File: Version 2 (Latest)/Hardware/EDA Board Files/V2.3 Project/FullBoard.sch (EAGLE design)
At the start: 187 parts, among them IC1 LM3914V, IC2 SGTL5000XNAA3, IC4 MCP73113-16SI_MF, IC5 NCP163ASN330T1G, J1 SJ-3524-SMT-TR, J10 SJ-3524-SMT-TR, J2 Teensy2, J3 Teensy1, J4 SJ-3524-SMT-TR, J7 1981584-1, J9 SJ-3524-SMT-TR, Q2 DMG9926USD-13, SW1 GATERON_LOW_PROFILE, SW10 GATERON_LOW_PROFILE, SW11 GATERON_LOW_PROFILE, SW12 GATERON_LOW_PROFILE, SW13 GATERON_LOW_PROFILE, SW14 GATERON_LOW_PROFILE, SW15 GATERON_LOW_PROFILE, SW16 GATERON_LOW_PROFILE, SW17 GATERON_LOW_PROFILE, SW18 GATERON_LOW_PROFILE, SW19 GATERON_LOW_PROFILE, SW2 GATERON_LOW_PROFILE, SW20 GATERON_LOW_PROFILE, SW21 GATERON_LOW_PROFILE, SW22 GATERON_LOW_PROFILE, SW23 GATERON_LOW_PROFILE, SW24 GATERON_LOW_PROFILE, SW25 GATERON_LOW_PROFILE, SW26 GATERON_LOW_PROFILE, SW27 GATERON_LOW_PROFILE, SW28 GATERON_LOW_PROFILE, SW29 GATERON_LOW_PROFILE, SW3 GATERON_LOW_PROFILE, SW30 GATERON_LOW_PROFILE, SW31 GATERON_LOW_PROFILE, SW32 GATERON_LOW_PROFILE, SW33 GATERON_LOW_PROFILE, SW34 GATERON_LOW_PROFILE, SW35 GATERON_LOW_PROFILE, SW36 GATERON_LOW_PROFILE, SW37 GATERON_LOW_PROFILE, SW38 GATERON_LOW_PROFILE, SW39 GATERON_LOW_PROFILE, SW4 GATERON_LOW_PROFILE, SW40 GATERON_LOW_PROFILE, SW41 GATERON_LOW_PROFILE, SW42 GATERON_LOW_PROFILE, SW43 GATERON_LOW_PROFILE, SW44 GATERON_LOW_PROFILE, SW45 GATERON_LOW_PROFILE, SW46 GATERON_LOW_PROFILE, SW47 GATERON_LOW_PROFILE, SW5 GATERON_LOW_PROFILE, SW6 GATERON_LOW_PROFILE, SW7 GATERON_LOW_PROFILE, SW8 GATERON_LOW_PROFILE, SW9 GATERON_LOW_PROFILE, U1 W25Q128FVSIG, U2 ATMEGA4809-AFR, U3 PAM2401, U4 MAX6775XKA+21-0076E_MXM-M, U5 AP7313-15SAG-7SOT-23_DIO-L, U6 S25FL512SAGMFIR13SO3016_SPA-M

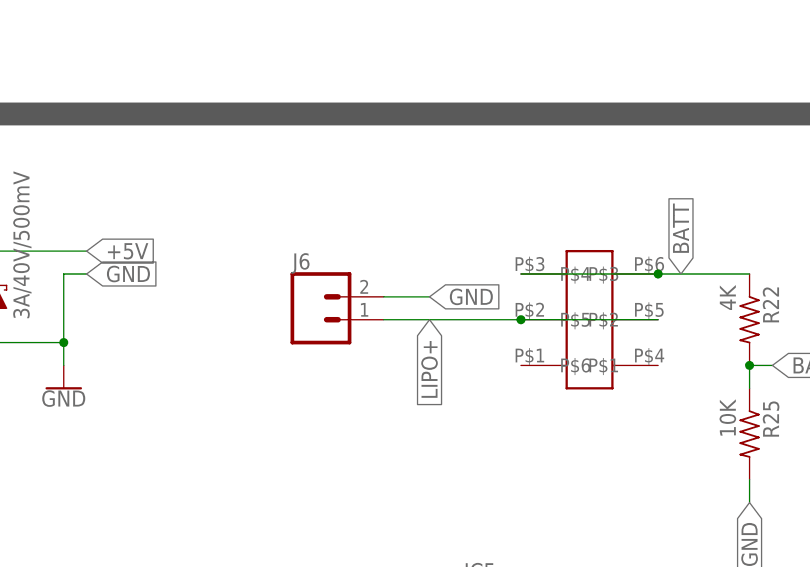
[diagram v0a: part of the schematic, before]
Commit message: Updated battery connector on PCB
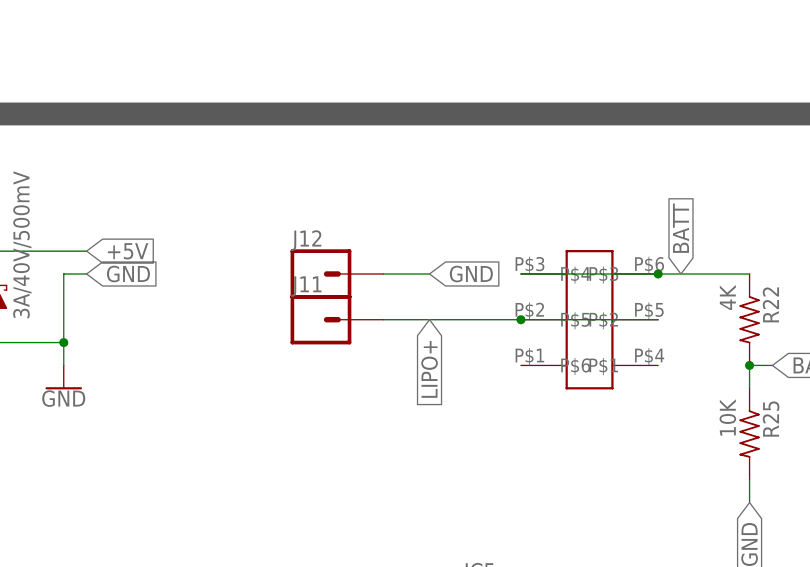
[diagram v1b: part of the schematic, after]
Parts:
- removed J6: (no value), SparkFun-Connectors:CONN_02
- added J11, J12: (no value), SparkFun-Connectors:CONN_01
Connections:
- net GND: now also J12.1; no longer J6.2
- net LIPO+: now also J11.1; no longer J6.1
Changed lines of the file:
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@@
 <part name="C22" library="SparkFun-Capacitors" library_urn="urn:adsk.eagle:library:510" deviceset="22UF" device="-0805-6.3V-20%" package3d_urn="urn:adsk.eagle:package:37429/1" value="22uF"/>
 <part name="CHARGE" library="adafruit" library_urn="urn:adsk.eagle:library:420" deviceset="LED" device="CHIPLED_0805" package3d_urn="urn:adsk.eagle:package:6240559/1"/>
-<part name="J6" library="SparkFun-Connectors" deviceset="CONN_02" device=""/>
 <part name="U4" library="BatteryStuff" deviceset="MAX6775XKA+" device="21-0076E_MXM-M"/>
 <part name="R21" library="adafruit" library_urn="urn:adsk.eagle:library:420" deviceset="R-US_" device="M0805" package3d_urn="urn:adsk.eagle:package:6240587/1" value="3.2M"/>
@@
 <part name="TP3" library="SparkFun-Connectors" library_urn="urn:adsk.eagle:library:513" deviceset="TEST-POINT" device="3X5" package3d_urn="urn:adsk.eagle:package:38285/1"/>
 <part name="TP4" library="SparkFun-Connectors" library_urn="urn:adsk.eagle:library:513" deviceset="TEST-POINT" device="3X5" package3d_urn="urn:adsk.eagle:package:38285/1"/>
+<part name="J11" library="SparkFun-Connectors" library_urn="urn:adsk.eagle:library:513" deviceset="CONN_01" device="" package3d_urn="urn:adsk.eagle:package:38028/1"/>
+<part name="J12" library="SparkFun-Connectors" library_urn="urn:adsk.eagle:library:513" deviceset="CONN_01" device="" package3d_urn="urn:adsk.eagle:package:38028/1"/>
 </parts>
 <sheets>
@@
 <attribute name="VALUE" x="-38.608" y="-235.585" size="1.778" layer="96" rot="R180"/>
 </instance>
-<instance part="J6" gate="G$1" x="-86.36" y="-144.78" smashed="yes">
-<attribute name="VALUE" x="-88.9" y="-149.606" size="1.778" layer="96" font="vector"/>
-<attribute name="NAME" x="-88.9" y="-139.192" size="1.778" layer="95" font="vector"/>
-</instance>
 <instance part="U4" gate="A" x="-241.3" y="-226.06" smashed="yes">
 <attribute name="NAME" x="-215.5444" y="-216.9414" size="2.0828" layer="95" ratio="6" rot="SR0"/>
@@
 <attribute name="NAME" x="-48.26" y="-73.66" size="1.778" layer="95" font="vector"/>
 <attribute name="VALUE" x="-48.26" y="-78.74" size="1.778" layer="96" font="vector"/>
+</instance>
+<instance part="J11" gate="G$1" x="-86.36" y="-144.78" smashed="yes">
+<attribute name="VALUE" x="-88.9" y="-149.606" size="1.778" layer="96" font="vector"/>
+<attribute name="NAME" x="-88.9" y="-141.732" size="1.778" layer="95" font="vector"/>
+</instance>
+<instance part="J12" gate="G$1" x="-86.36" y="-139.7" smashed="yes">
+<attribute name="VALUE" x="-88.9" y="-144.526" size="1.778" layer="96" font="vector"/>
+<attribute name="NAME" x="-88.9" y="-136.652" size="1.778" layer="95" font="vector"/>
 </instance>
 </instances>
@@
 </segment>
 <segment>
-<pinref part="J6" gate="G$1" pin="2"/>
-<wire x1="-78.74" y1="-142.24" x2="-73.66" y2="-142.24" width="0.1524" layer="91"/>
-<label x="-73.66" y="-142.24" size="1.778" layer="95" xref="yes"/>
+<wire x1="-78.74" y1="-139.7" x2="-73.66" y2="-139.7" width="0.1524" layer="91"/>
+<label x="-73.66" y="-139.7" size="1.778" layer="95" xref="yes"/>
+<pinref part="J12" gate="G$1" pin="1"/>
 </segment>
 <segment>
@@
 <net name="LIPO+" class="0">
 <segment>
-<pinref part="J6" gate="G$1" pin="1"/>
 <wire x1="-78.74" y1="-144.78" x2="-63.5" y2="-144.78" width="0.1524" layer="91"/>
 <pinref part="U$1" gate="G$1" pin="P$2"/>
@@
 <junction x="-63.5" y="-144.78"/>
 <label x="-73.66" y="-144.78" size="1.778" layer="95" rot="R270" xref="yes"/>
-</segment>
-<segment>
+<pinref part="J11" gate="G$1" pin="1"/>
+</segment>
+<segment>
